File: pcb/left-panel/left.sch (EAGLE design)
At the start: 4 parts, among them J1 SNG-2MM-HEADER-04-V, SW1 B3F-315X, SW2 B3F-315X, SW3 B3F-315X

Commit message: Display base pcb (rev C), Touch panel (rev B)
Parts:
- SW1, SW2, SW3: value B3F-315X -> B3F-3150; device Switch:B3F-315X -> Switch:B3F-3150
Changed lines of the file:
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@@
 <parts>
 <part name="FRAME1" library="Symbols" deviceset="FRAME_ANSI_B" device=""/>
-<part name="SW1" library="Switch" deviceset="B3F-315X" device="">
+<part name="SW1" library="Switch" deviceset="B3F-315?" device="" technology="0">
 <attribute name="PRICE" value="0.21"/>
 </part>
-<part name="SW2" library="Switch" deviceset="B3F-315X" device="">
+<part name="SW2" library="Switch" deviceset="B3F-315?" device="" technology="0">
 <attribute name="PRICE" value="0.21"/>
 <attribute name="TEST" value="test"/>
 </part>
-<part name="SW3" library="Switch" deviceset="B3F-315X" device="">
+<part name="SW3" library="Switch" deviceset="B3F-315?" device="" technology="0">
 <attribute name="PRICE" value="0.21"/>
 </part>

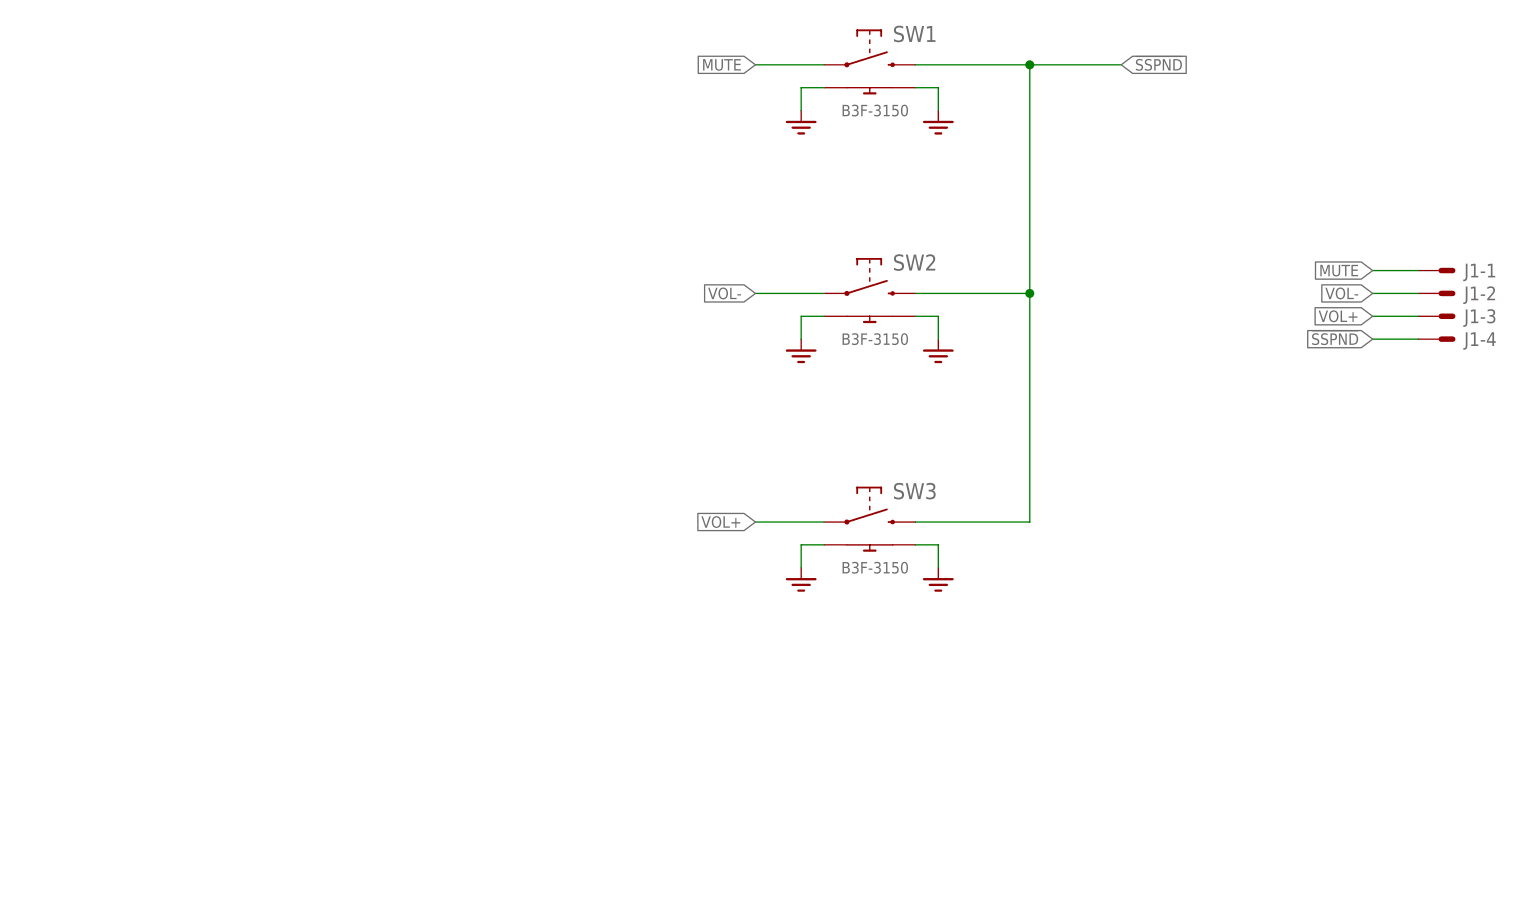
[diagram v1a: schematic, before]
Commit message: Changed page format on schematics to US letter (8.5" x 11")
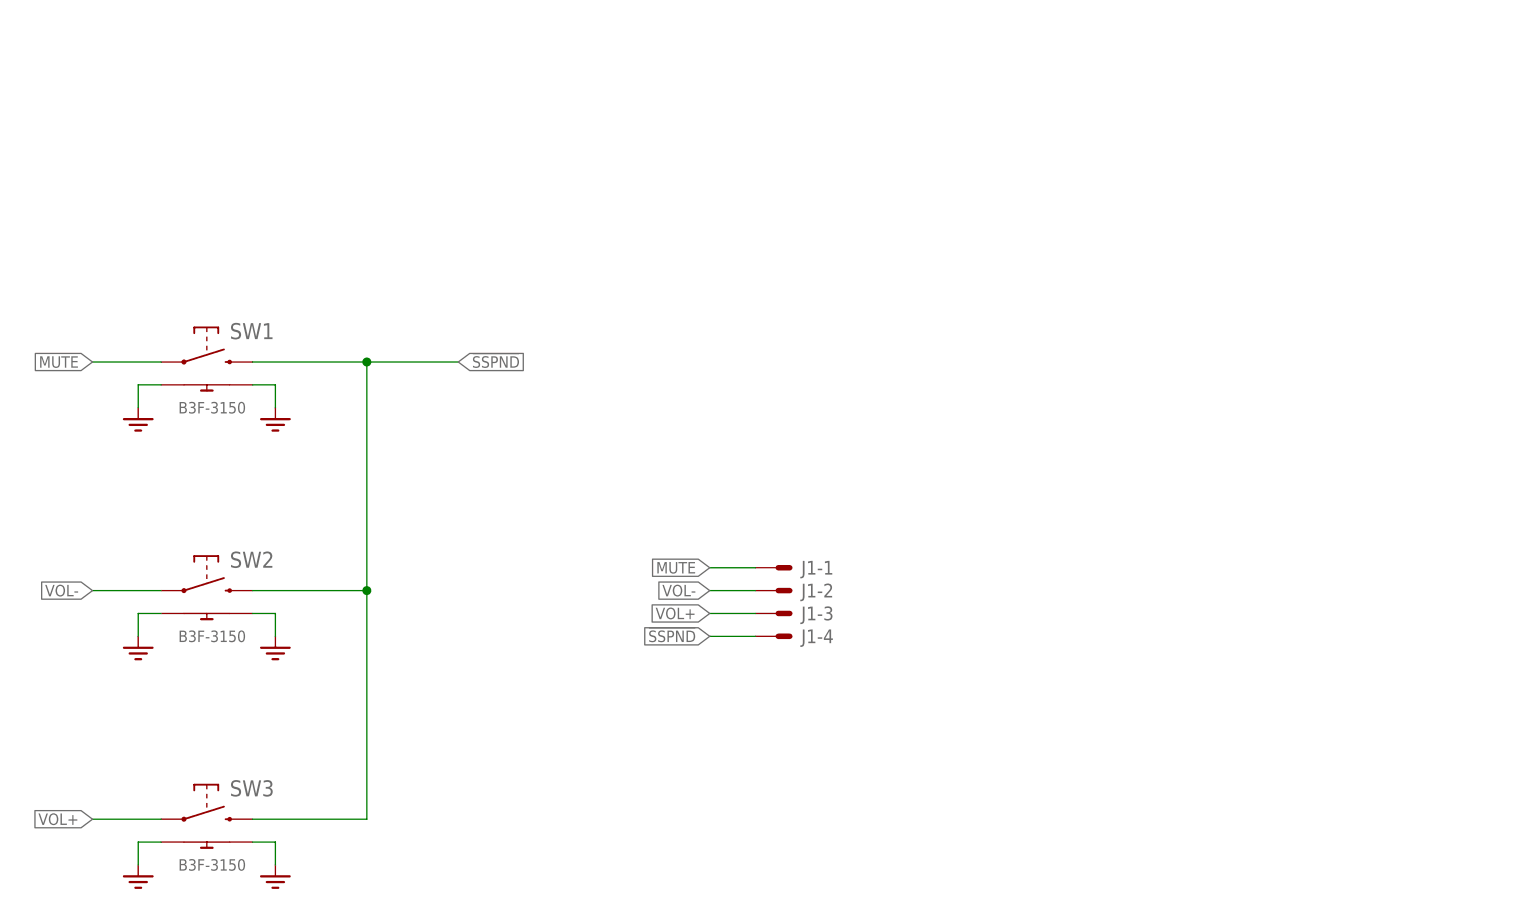
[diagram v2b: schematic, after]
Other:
- moved on the sheet: J1-1, J1-2, J1-3, J1-4, SW1, SW2, SW3
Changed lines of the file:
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@@
 </classes>
 <parts>
-<part name="FRAME1" library="Symbols" deviceset="FRAME_ANSI_B" device=""/>
+<part name="FRAME1" library="Symbols" deviceset="FRAME_LETTER" device=""/>
 <part name="SW1" library="Switch" deviceset="B3F-315?" device="" technology="0">
 <attribute name="PRICE" value="0.21"/>
@@
 <instances>
 <instance part="FRAME1" gate="G$1" x="0" y="0"/>
-<instance part="SW1" gate="G$1" x="182.88" y="162.56">
-<attribute name="PRICE" x="182.88" y="162.56" size="1.778" layer="96" display="off"/>
+<instance part="SW1" gate="G$1" x="109.22" y="129.54">
+<attribute name="PRICE" x="109.22" y="129.54" size="1.778" layer="96" display="off"/>
 </instance>
-<instance part="SW2" gate="G$1" x="182.88" y="137.16">
-<attribute name="TEST" x="182.88" y="137.16" size="1.27" layer="96" display="off"/>
-<attribute name="PRICE" x="182.88" y="137.16" size="1.778" layer="96" display="off"/>
+<instance part="SW2" gate="G$1" x="109.22" y="104.14">
+<attribute name="TEST" x="109.22" y="104.14" size="1.27" layer="96" display="off"/>
+<attribute name="PRICE" x="109.22" y="104.14" size="1.778" layer="96" display="off"/>
 </instance>
-<instance part="SW3" gate="G$1" x="182.88" y="111.76">
-<attribute name="PRICE" x="182.88" y="111.76" size="1.778" layer="96" display="off"/>
+<instance part="SW3" gate="G$1" x="109.22" y="78.74">
+<attribute name="PRICE" x="109.22" y="78.74" size="1.778" layer="96" display="off"/>
 </instance>
-<instance part="GND1" gate="GND" x="190.5" y="154.94"/>
-<instance part="GND2" gate="GND" x="175.26" y="154.94"/>
-<instance part="GND3" gate="GND" x="175.26" y="129.54"/>
-<instance part="GND4" gate="GND" x="190.5" y="129.54"/>
-<instance part="GND5" gate="GND" x="175.26" y="104.14"/>
-<instance part="GND6" gate="GND" x="190.5" y="104.14"/>
-<instance part="J1" gate="-1" x="246.38" y="139.7"/>
-<instance part="J1" gate="-2" x="246.38" y="137.16"/>
-<instance part="J1" gate="-3" x="246.38" y="134.62"/>
-<instance part="J1" gate="-4" x="246.38" y="132.08"/>
+<instance part="GND1" gate="GND" x="116.84" y="121.92"/>
+<instance part="GND2" gate="GND" x="101.6" y="121.92"/>
+<instance part="GND3" gate="GND" x="101.6" y="96.52"/>
+<instance part="GND4" gate="GND" x="116.84" y="96.52"/>
+<instance part="GND5" gate="GND" x="101.6" y="71.12"/>
+<instance part="GND6" gate="GND" x="116.84" y="71.12"/>
+<instance part="J1" gate="-1" x="172.72" y="106.68"/>
+<instance part="J1" gate="-2" x="172.72" y="104.14"/>
+<instance part="J1" gate="-3" x="172.72" y="101.6"/>
+<instance part="J1" gate="-4" x="172.72" y="99.06"/>
 </instances>
 <busses>
@@
 <pinref part="SW1" gate="G$1" pin="3"/>
 <pinref part="GND2" gate="GND" pin="GND"/>
-<wire x1="177.8" y1="160.02" x2="175.26" y2="160.02" width="0.1524" layer="91"/>
-<wire x1="175.26" y1="160.02" x2="175.26" y2="157.48" width="0.1524" layer="91"/>
+<wire x1="104.14" y1="127" x2="101.6" y2="127" width="0.1524" layer="91"/>
+<wire x1="101.6" y1="127" x2="101.6" y2="124.46" width="0.1524" layer="91"/>
 </segment>
 <segment>
 <pinref part="SW1" gate="G$1" pin="4"/>
 <pinref part="GND1" gate="GND" pin="GND"/>
-<wire x1="187.96" y1="160.02" x2="190.5" y2="160.02" width="0.1524" layer="91"/>
-<wire x1="190.5" y1="160.02" x2="190.5" y2="157.48" width="0.1524" layer="91"/>
+<wire x1="114.3" y1="127" x2="116.84" y2="127" width="0.1524" layer="91"/>
+<wire x1="116.84" y1="127" x2="116.84" y2="124.46" width="0.1524" layer="91"/>
 </segment>
 <segment>
 <pinref part="SW2" gate="G$1" pin="3"/>
 <pinref part="GND3" gate="GND" pin="GND"/>
-<wire x1="177.8" y1="134.62" x2="175.26" y2="134.62" width="0.1524" layer="91"/>
-<wire x1="175.26" y1="134.62" x2="175.26" y2="132.08" width="0.1524" layer="91"/>
+<wire x1="104.14" y1="101.6" x2="101.6" y2="101.6" width="0.1524" layer="91"/>
+<wire x1="101.6" y1="101.6" x2="101.6" y2="99.06" width="0.1524" layer="91"/>
 </segment>
 <segment>
 <pinref part="SW2" gate="G$1" pin="4"/>
 <pinref part="GND4" gate="GND" pin="GND"/>
-<wire x1="187.96" y1="134.62" x2="190.5" y2="134.62" width="0.1524" layer="91"/>
-<wire x1="190.5" y1="134.62" x2="190.5" y2="132.08" width="0.1524" layer="91"/>
+<wire x1="114.3" y1="101.6" x2="116.84" y2="101.6" width="0.1524" layer="91"/>
+<wire x1="116.84" y1="101.6" x2="116.84" y2="99.06" width="0.1524" layer="91"/>
 </segment>
 <segment>
 <pinref part="SW3" gate="G$1" pin="3"/>
 <pinref part="GND5" gate="GND" pin="GND"/>
-<wire x1="177.8" y1="109.22" x2="175.26" y2="109.22" width="0.1524" layer="91"/>
-<wire x1="175.26" y1="109.22" x2="175.26" y2="106.68" width="0.1524" layer="91"/>
+<wire x1="104.14" y1="76.2" x2="101.6" y2="76.2" width="0.1524" layer="91"/>
+<wire x1="101.6" y1="76.2" x2="101.6" y2="73.66" width="0.1524" layer="91"/>
 </segment>
 <segment>
 <pinref part="SW3" gate="G$1" pin="4"/>
 <pinref part="GND6" gate="GND" pin="GND"/>
-<wire x1="187.96" y1="109.22" x2="190.5" y2="109.22" width="0.1524" layer="91"/>
-<wire x1="190.5" y1="109.22" x2="190.5" y2="106.68" width="0.1524" layer="91"/>
+<wire x1="114.3" y1="76.2" x2="116.84" y2="76.2" width="0.1524" layer="91"/>
+<wire x1="116.84" y1="76.2" x2="116.84" y2="73.66" width="0.1524" layer="91"/>
 </segment>
 </net>
@@
 <segment>
 <pinref part="SW3" gate="G$1" pin="2"/>
-<wire x1="187.96" y1="111.76" x2="200.66" y2="111.76" width="0.1524" layer="91"/>
-<wire x1="200.66" y1="111.76" x2="200.66" y2="137.16" width="0.1524" layer="91"/>
+<wire x1="114.3" y1="78.74" x2="127" y2="78.74" width="0.1524" layer="91"/>
+<wire x1="127" y1="78.74" x2="127" y2="104.14" width="0.1524" layer="91"/>
 <pinref part="SW2" gate="G$1" pin="2"/>
-<wire x1="200.66" y1="137.16" x2="187.96" y2="137.16" width="0.1524" layer="91"/>
-<wire x1="200.66" y1="137.16" x2="200.66" y2="162.56" width="0.1524" layer="91"/>
-<junction x="200.66" y="137.16"/>
+<wire x1="127" y1="104.14" x2="114.3" y2="104.14" width="0.1524" layer="91"/>
+<wire x1="127" y1="104.14" x2="127" y2="129.54" width="0.1524" layer="91"/>
+<junction x="127" y="104.14"/>
 <pinref part="SW1" gate="G$1" pin="2"/>
-<wire x1="200.66" y1="162.56" x2="187.96" y2="162.56" width="0.1524" layer="91"/>
-<wire x1="200.66" y1="162.56" x2="210.82" y2="162.56" width="0.1524" layer="91"/>
-<junction x="200.66" y="162.56"/>
-<label x="210.82" y="162.56" size="1.27" layer="95" xref="yes"/>
+<wire x1="127" y1="129.54" x2="114.3" y2="129.54" width="0.1524" layer="91"/>
+<wire x1="127" y1="129.54" x2="137.16" y2="129.54" width="0.1524" layer="91"/>
+<junction x="127" y="129.54"/>
+<label x="137.16" y="129.54" size="1.27" layer="95" xref="yes"/>
 </segment>
 <segment>
 <pinref part="J1" gate="-4" pin="S"/>
-<wire x1="243.84" y1="132.08" x2="238.76" y2="132.08" width="0.1524" layer="91"/>
-<label x="238.76" y="132.08" size="1.27" layer="95" rot="R180" xref="yes"/>
+<wire x1="170.18" y1="99.06" x2="165.1" y2="99.06" width="0.1524" layer="91"/>
+<label x="165.1" y="99.06" size="1.27" layer="95" rot="R180" xref="yes"/>
 </segment>
 </net>
@@
 <segment>
 <pinref part="SW1" gate="G$1" pin="1"/>
-<wire x1="177.8" y1="162.56" x2="170.18" y2="162.56" width="0.1524" layer="91"/>
-<label x="170.18" y="162.56" size="1.27" layer="95" rot="R180" xref="yes"/>
+<wire x1="104.14" y1="129.54" x2="96.52" y2="129.54" width="0.1524" layer="91"/>
+<label x="96.52" y="129.54" size="1.27" layer="95" rot="R180" xref="yes"/>
 </segment>
 <segment>
 <pinref part="J1" gate="-1" pin="S"/>
-<wire x1="243.84" y1="139.7" x2="238.76" y2="139.7" width="0.1524" layer="91"/>
-<label x="238.76" y="139.7" size="1.27" layer="95" rot="R180" xref="yes"/>
+<wire x1="170.18" y1="106.68" x2="165.1" y2="106.68" width="0.1524" layer="91"/>
+<label x="165.1" y="106.68" size="1.27" layer="95" rot="R180" xref="yes"/>
 </segment>
 </net>
@@
 <segment>
 <pinref part="SW2" gate="G$1" pin="1"/>
-<wire x1="177.8" y1="137.16" x2="170.18" y2="137.16" width="0.1524" layer="91"/>
-<label x="170.18" y="137.16" size="1.27" layer="95" rot="R180" xref="yes"/>
+<wire x1="104.14" y1="104.14" x2="96.52" y2="104.14" width="0.1524" layer="91"/>
+<label x="96.52" y="104.14" size="1.27" layer="95" rot="R180" xref="yes"/>
 </segment>
 <segment>
 <pinref part="J1" gate="-2" pin="S"/>
-<wire x1="243.84" y1="137.16" x2="238.76" y2="137.16" width="0.1524" layer="91"/>
-<label x="238.76" y="137.16" size="1.27" layer="95" rot="R180" xref="yes"/>
+<wire x1="170.18" y1="104.14" x2="165.1" y2="104.14" width="0.1524" layer="91"/>
+<label x="165.1" y="104.14" size="1.27" layer="95" rot="R180" xref="yes"/>
 </segment>
 </net>
@@
 <segment>
 <pinref part="SW3" gate="G$1" pin="1"/>
-<wire x1="177.8" y1="111.76" x2="170.18" y2="111.76" width="0.1524" layer="91"/>
-<label x="170.18" y="111.76" size="1.27" layer="95" rot="R180" xref="yes"/>
+<wire x1="104.14" y1="78.74" x2="96.52" y2="78.74" width="0.1524" layer="91"/>
+<label x="96.52" y="78.74" size="1.27" layer="95" rot="R180" xref="yes"/>
 </segment>
 <segment>
 <pinref part="J1" gate="-3" pin="S"/>
-<wire x1="243.84" y1="134.62" x2="238.76" y2="134.62" width="0.1524" layer="91"/>
-<label x="238.76" y="134.62" size="1.27" layer="95" rot="R180" xref="yes"/>
+<wire x1="170.18" y1="101.6" x2="165.1" y2="101.6" width="0.1524" layer="91"/>
+<label x="165.1" y="101.6" size="1.27" layer="95" rot="R180" xref="yes"/>
 </segment>
 </net>
